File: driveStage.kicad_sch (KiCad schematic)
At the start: 57 parts, among them J1 MOD_IN, J2 DNP, J3 DNP, Q1 CSD17507Q5A, SW1 SW_DIP_x03, U1 LTC6655BHLS8-4.096, U2 MAX5719xSD, U3 ADA4898-1YRDZ, U4 ADA4898-1YRDZ, U5 RS8552, U6 ADA4898-1YRDZ

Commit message: complete placement
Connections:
- net GND: no longer J3.1 (In), R13.3
- new net: J3.1 (In), R13.3
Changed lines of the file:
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@@
   (junction (at 71.12 106.68) (diameter 0) (color 0 0 0 0)
   )
-  (junction (at 374.65 124.46) (diameter 0) (color 0 0 0 0)
-  )
   (junction (at 334.01 78.74) (diameter 0) (color 0 0 0 0)
   )
@@
   )
   (junction (at 118.11 119.38) (diameter 0) (color 0 0 0 0)
-  )
-  (junction (at 368.3 124.46) (diameter 0) (color 0 0 0 0)
   )
   (junction (at 341.63 196.85) (diameter 0) (color 0 0 0 0)
@@
     (stroke (width 0) (type default) (color 0 0 0 0))
   )
-  (wire (pts (xy 368.3 121.92) (xy 368.3 124.46))
+  (wire (pts (xy 368.3 121.92) (xy 368.3 161.29))
     (stroke (width 0) (type default) (color 0 0 0 0))
   )
@@
     (stroke (width 0) (type default) (color 0 0 0 0))
   )
-  (wire (pts (xy 368.3 124.46) (xy 368.3 161.29))
-    (stroke (width 0) (type default) (color 0 0 0 0))
-  )
   (wire (pts (xy 205.74 114.3) (xy 210.82 114.3))
     (stroke (width 0) (type default) (color 0 0 0 0))
@@
     (stroke (width 0) (type default) (color 0 0 0 0))
   )
-  (wire (pts (xy 368.3 124.46) (xy 374.65 124.46))
-    (stroke (width 0) (type default) (color 0 0 0 0))
-  )

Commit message: more routing
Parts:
- removed TP1, TP2, TP3, TP36, TP37, TP38, TP4, TP5, TP6, TP7, TP8: TestPoint, TestPoint:TestPoint_Pad_2.0x2.0mm, symbol Connector:TestPoint

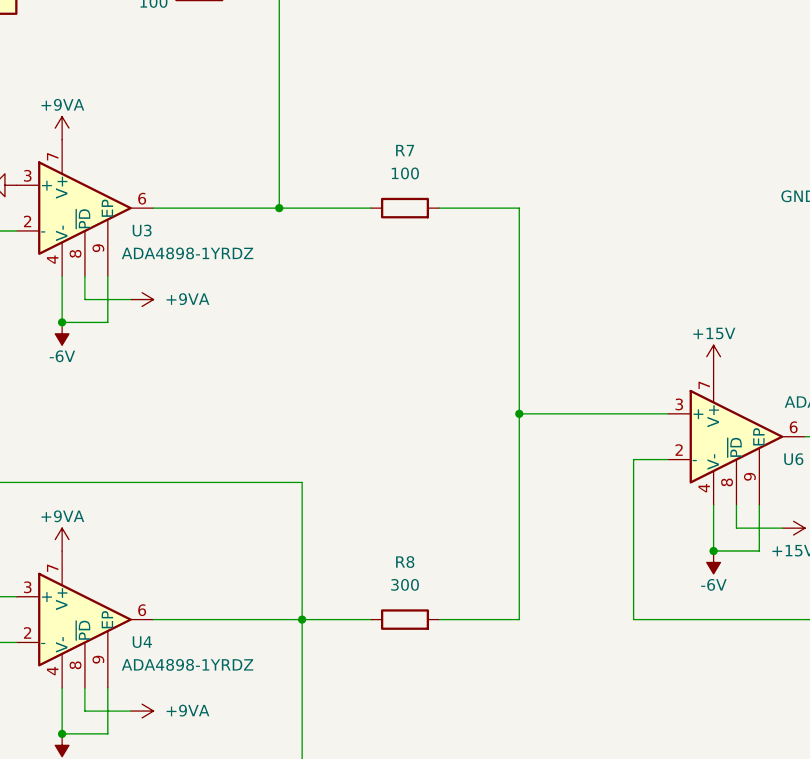
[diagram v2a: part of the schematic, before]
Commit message: add V01 production files, bug fixes
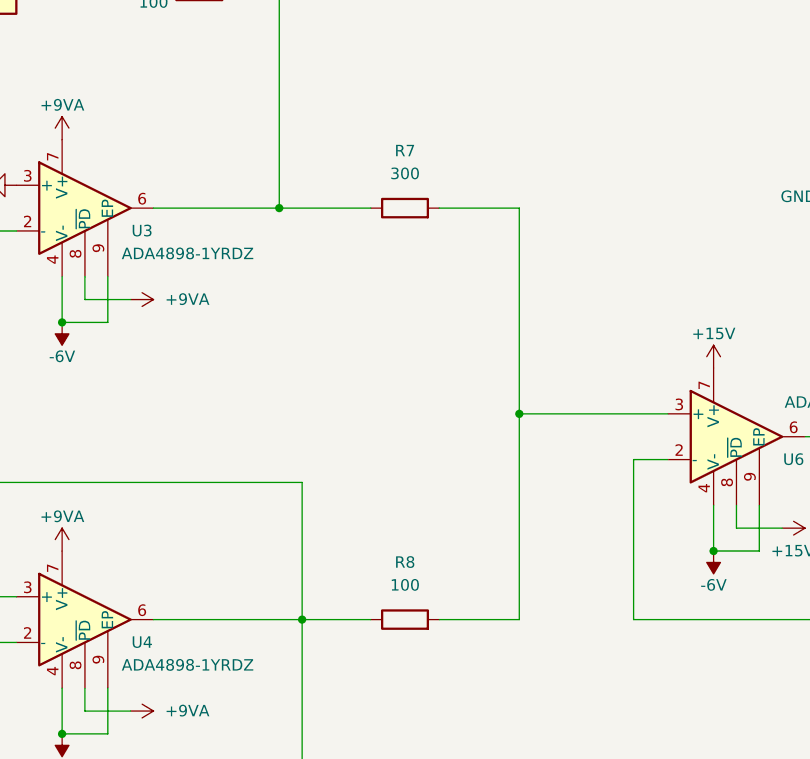
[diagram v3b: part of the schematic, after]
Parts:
- R7: value 100 -> 300
- R8: value 300 -> 100
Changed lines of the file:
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@@
     (in_bom yes) (on_board yes) (fields_autoplaced)
     (property "Reference" "R8" (id 0) (at 284.48 110.49 90))
-    (property "Value" "300" (id 1) (at 284.48 113.03 90))
+    (property "Value" "100" (id 1) (at 284.48 113.03 90))
     (property "Footprint" "Resistor_SMD:R_0603_1608Metric" (id 2) (at 284.48 118.618 90)
       (effects (font (size 1.27 1.27)) hide)
@@
     (in_bom yes) (on_board yes) (fields_autoplaced)
     (property "Reference" "R7" (id 0) (at 284.48 64.77 90))
-    (property "Value" "100" (id 1) (at 284.48 67.31 90))
+    (property "Value" "300" (id 1) (at 284.48 67.31 90))
     (property "Footprint" "Resistor_SMD:R_0603_1608Metric" (id 2) (at 284.48 72.898 90)
       (effects (font (size 1.27 1.27)) hide)

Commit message: v 0.2 schematics
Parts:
- removed J2, J3: DNP, Connector_Coaxial:U.FL_Hirose_U.FL-R-SMT-1_Vertical, symbol Connector:Conn_Coaxial
- removed R1: 50, Resistor_SMD:R_0805_2012Metric, symbol Device:R
- removed R2, R6: 100, Resistor_SMD:R_0603_1608Metric, symbol Device:R
- removed R5: 10, Resistor_SMD:R_0603_1608Metric, symbol Device:R
- added C? (x2): DNP, Capacitor_SMD:C_0603_1608Metric, symbol Device:C
- added C?: 10u PP, Capacitor_SMD:C_1812_4532Metric, symbol Device:C
- added C? (x2): 100n PPS, Capacitor_SMD:C_1210_3225Metric, symbol Device:C
- added R? (x2): DNP, Resistor_SMD:R_0603_1608Metric, symbol Device:R
- added R? (x2): 10, Resistor_SMD:R_0603_1608Metric, symbol Device:R
- added R?: 99, symbol Device:R
- added R?: 90, symbol Device:R
- added TP1, TP2, TP3, TP36, TP37, TP38, TP4: TestPoint, TestPoint:TestPoint_Pad_2.0x2.0mm, symbol Connector:TestPoint
- Q1: value CSD17507Q5A -> SQJA70EP-T1; MFR_PN CSD17507Q5A -> SQJA70EP-T1_GE3
- R13: footprint Resistor_SMD:R_Shunt_Ohmite_LVK20 -> kirdy:R_Shunt_VCS1625ZP
- R7: value 300 -> 100
- R8: value 100 -> 300
- renumbered C172 to C?
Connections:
- net DIN: now also TP3.1
- net GND: now also R13.3, R4.1, C?.2, C?.2, C?.2, R?.1; no longer U3.3 (+)
- net LD-: now also R?.2
- net PD_BIAS: now also TP38.1
- net PD_C: now also TP37.1
- net PD_MON: now also TP36.1
- net SCLK: now also TP2.1
- net ~{CS}: now also TP4.1
- net ~{LDAC}: now also TP1.1
- net at SW1.4: now also SW1.5, SW1.6, U3.3 (+)
- net at R7.1, U3.6: now also U3.2 (-); no longer R4.2
- net at R10.2, R11.1, TP9.1: now also C?.2
- net at C13.2, R10.1, U6.2 (-): now also R?.1, R?.1
- net at R7.2, R8.2, U6.3 (+): now also C?.1, C?.1
- net at C13.1, Q1.4 (G), U6.6: now also C?.1
- net at J1.1 (In): now also D1.2 (A2), SW1.1, R?.1, R?.1
- new net: C?.2, R?.2
- new net: C?.1, R?.1
- new net: R?.2, R?.2, SW1.2
- new net: R4.2, R?.2, SW1.3
- new net: C?.1, R?.2
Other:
- note removed: "For noise measurement"
- moved on the sheet: C1, C10, C11, C12, C13, C15, C16, C2, C3, C4, C5, C6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

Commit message: fixes
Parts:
- removed C?: 100n PPS, Capacitor_SMD:C_1210_3225Metric, symbol Device:C
- removed TP1, TP2, TP3, TP4: TestPoint, TestPoint:TestPoint_Pad_2.0x2.0mm, symbol Connector:TestPoint
- added C?: 10u PP, Capacitor_SMD:C_1812_4532Metric, symbol Device:C
- added R?: 100, Resistor_SMD:R_0603_1608Metric, symbol Device:R
- R7: value 100 -> 300
- R8: value 300 -> 100
- R?: value 10 -> 3.3; MFR_PN RT0603BRD0710RL -> (none); MFR_PN_ALT WR06X10R0FTL -> (none)
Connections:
- net GND: now also C?.2
- net at C5.2, R8.1, U4.2 (-): now also C?.1, C?.1, R?.2; no longer U4.6
- net at R?.1: now also C?.1
- net at R7.2, R8.2, U6.3 (+): no longer C?.1, C?.1
- new net: R?.1, U4.6
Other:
- moved on the sheet: C?, R8

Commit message: compensation
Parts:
- added C?: 1n6, Capacitor_SMD:C_0603_1608Metric, symbol Device:C
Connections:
- net at C5.2, C?.1, C?.1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: now also C?.1
- net at R?.1, U4.6: now also C?.2
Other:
- moved on the sheet: R?
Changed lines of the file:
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@@
   (junction (at 347.98 229.87) (diameter 0) (color 0 0 0 0)
   )
+  (junction (at 223.52 116.84) (diameter 0) (color 0 0 0 0)
+  )
   (junction (at 351.79 205.74) (diameter 0) (color 0 0 0 0)
   )
@@
   )
   (junction (at 116.84 127) (diameter 0) (color 0 0 0 0)
+  )
+  (junction (at 229.87 137.16) (diameter 0) (color 0 0 0 0)
   )
   (junction (at 24.13 106.68) (diameter 0) (color 0 0 0 0)
@@
     (stroke (width 0) (type default) (color 0 0 0 0))
   )
-  (wire (pts (xy 213.36 127) (xy 218.44 127))
+  (wire (pts (xy 213.36 127) (xy 217.17 127))
     (stroke (width 0) (type default) (color 0 0 0 0))
   )
@@
     (stroke (width 0) (type default) (color 0 0 0 0))
   )
+  (wire (pts (xy 229.87 137.16) (xy 237.49 137.16))
+    (stroke (width 0) (type default) (color 0 0 0 0))
+  )
   (wire (pts (xy 175.26 114.3) (xy 205.74 114.3))
     (stroke (width 0) (type default) (color 0 0 0 0))
@@
     (stroke (width 0) (type default) (color 0 0 0 0))
   )
-  (wire (pts (xy 233.68 116.84) (xy 237.49 116.84))
+  (wire (pts (xy 234.95 116.84) (xy 237.49 116.84))
     (stroke (width 0) (type default) (color 0 0 0 0))
   )
@@
     (stroke (width 0) (type default) (color 0 0 0 0))
   )
-  (wire (pts (xy 200.66 137.16) (xy 237.49 137.16))
+  (wire (pts (xy 200.66 137.16) (xy 229.87 137.16))
     (stroke (width 0) (type default) (color 0 0 0 0))
   )
@@
     (stroke (width 0) (type default) (color 0 0 0 0))
   )
+  (wire (pts (xy 229.87 120.65) (xy 223.52 120.65))
+    (stroke (width 0) (type default) (color 0 0 0 0))
+  )
   (wire (pts (xy 88.9 106.68) (xy 104.14 106.68))
     (stroke (width 0) (type default) (color 0 0 0 0))
@@
     (stroke (width 0) (type default) (color 0 0 0 0))
   )
+  (wire (pts (xy 223.52 120.65) (xy 223.52 116.84))
+    (stroke (width 0) (type default) (color 0 0 0 0))
+  )
   (wire (pts (xy 341.63 109.22) (xy 341.63 116.84))
     (stroke (width 0) (type default) (color 0 0 0 0))
@@
     (stroke (width 0) (type default) (color 0 0 0 0))
   )
+  (wire (pts (xy 229.87 130.81) (xy 229.87 137.16))
+    (stroke (width 0) (type default) (color 0 0 0 0))
+  )
   (wire (pts (xy 299.72 63.5) (xy 299.72 64.77))
     (stroke (width 0) (type default) (color 0 0 0 0))
@@
     (stroke (width 0) (type default) (color 0 0 0 0))
   )
+  (wire (pts (xy 223.52 116.84) (xy 227.33 116.84))
+    (stroke (width 0) (type default) (color 0 0 0 0))
+  )
   (wire (pts (xy 360.68 124.46) (xy 367.03 124.46))
     (stroke (width 0) (type default) (color 0 0 0 0))
@@
     (stroke (width 0) (type default) (color 0 0 0 0))
   )
+  (wire (pts (xy 229.87 123.19) (xy 229.87 120.65))
+    (stroke (width 0) (type default) (color 0 0 0 0))
+  )
   (wire (pts (xy 285.75 73.66) (xy 299.72 73.66))
     (stroke (width 0) (type default) (color 0 0 0 0))
   )
-  (wire (pts (xy 220.98 116.84) (xy 226.06 116.84))
+  (wire (pts (xy 220.98 116.84) (xy 223.52 116.84))
     (stroke (width 0) (type default) (color 0 0 0 0))
   )
@@
   (symbol (lib_id "Amplifier_Operational:ADA4898-1YRDZ") (at 213.36 116.84 0) (unit 1)
     (in_bom yes) (on_board yes)
-    (property "Reference" "U4" (id 0) (at 219.71 119.38 0))
-    (property "Value" "ADA4898-1YRDZ" (id 1) (at 224.79 121.92 0))
+    (property "Reference" "U4" (id 0) (at 218.44 110.49 0))
+    (property "Value" "ADA4898-1YRDZ" (id 1) (at 223.52 107.95 0))
     (property "Footprint" "Package_SO:SOIC-8-1EP_3.9x4.9mm_P1.27mm_EP2.29x3mm" (id 2) (at 213.36 132.08 0)
       (effects (font (size 1.27 1.27)) hide)
@@
     (pin "2")
   )
+  (symbol (lib_id "Device:C") (at 229.87 127 180) (unit 1)
+    (in_bom yes) (on_board yes)
+    (property "Reference" "C?" (id 0) (at 234.95 125.73 0))
+    (property "Value" "1n6" (id 1) (at 234.95 128.27 0))
+    (property "Footprint" "Capacitor_SMD:C_0603_1608Metric" (id 2) (at 228.9048 123.19 0)
+      (effects (font (size 1.27 1.27)) hide)
+    )
+    (property "Datasheet" "~" (id 3) (at 229.87 127 0)
+      (effects (font (size 1.27 1.27)) hide)
+    )
+    (property "MFR_PN" "GCM1885C1H162FA16D" (id 4) (at 229.87 127 0)
+      (effects (font (size 1.27 1.27)) hide)
+    )
+    (property "MFR_PN_ALT" "C0603C162J5GAC7867" (id 5) (at 229.87 127 0)
+      (effects (font (size 1.27 1.27)) hide)
+    )
+    (pin "1")
+    (pin "2")
+  )
   (symbol (lib_id "Device:C") (at 222.25 148.59 90) (unit 1)
     (in_bom yes) (on_board yes)
@@
     (pin "2")
   )
-  (symbol (lib_id "power:+9VA") (at 218.44 127 270) (unit 1)
-    (in_bom yes) (on_board yes) (fields_autoplaced)
-    (property "Reference" "#PWR021" (id 0) (at 215.265 127 0)
-      (effects (font (size 1.27 1.27)) hide)
-    )
-    (property "Value" "+9VA" (id 1) (at 222.25 126.9999 90)
-      (effects (font (size 1.27 1.27)) (justify left))
-    )
-    (property "Footprint" "" (id 2) (at 218.44 127 0)
-      (effects (font (size 1.27 1.27)) hide)
-    )
-    (property "Datasheet" "" (id 3) (at 218.44 127 0)
+  (symbol (lib_id "power:+9VA") (at 217.17 127 270) (unit 1)
+    (in_bom yes) (on_board yes) (fields_autoplaced)
+    (property "Reference" "#PWR021" (id 0) (at 213.995 127 0)
+      (effects (font (size 1.27 1.27)) hide)
+    )
+    (property "Value" "+9VA" (id 1) (at 220.98 126.9999 90)
+      (effects (font (size 1.27 1.27)) (justify left))
+    )
+    (property "Footprint" "" (id 2) (at 217.17 127 0)
+      (effects (font (size 1.27 1.27)) hide)
+    )
+    (property "Datasheet" "" (id 3) (at 217.17 127 0)
       (effects (font (size 1.27 1.27)) hide)
     )
@@
     (pin "2")
   )
-  (symbol (lib_id "Device:R") (at 229.87 116.84 90) (unit 1)
-    (in_bom yes) (on_board yes) (fields_autoplaced)
-    (property "Reference" "R?" (id 0) (at 229.87 110.49 90))
-    (property "Value" "100" (id 1) (at 229.87 113.03 90))
-    (property "Footprint" "Resistor_SMD:R_0603_1608Metric" (id 2) (at 229.87 118.618 90)
-      (effects (font (size 1.27 1.27)) hide)
-    )
-    (property "Datasheet" "~" (id 3) (at 229.87 116.84 0)
-      (effects (font (size 1.27 1.27)) hide)
-    )
-    (property "MFR_PN" "RT0603FRE07300RL" (id 4) (at 229.87 116.84 0)
-      (effects (font (size 1.27 1.27)) hide)
-    )
-    (property "MFR_PN_ALT" "RC0603FR-10300RL" (id 5) (at 229.87 116.84 0)
-      (effects (font (size 1.27 1.27)) hide)
-    )
+  (symbol (lib_id "Device:R") (at 231.14 116.84 90) (unit 1)
+    (in_bom yes) (on_board yes)
+    (property "Reference" "R?" (id 0) (at 231.14 111.76 90))
+    (property "Value" "100" (id 1) (at 231.14 114.3 90))
+    (property "Footprint" "Resistor_SMD:R_0603_1608Metric" (id 2) (at 231.14 118.618 90)
+      (effects (font (size 1.27 1.27)) hide)
+    )
+    (property "Datasheet" "~" (id 3) (at 231.14 116.84 0)
+      (effects (font (size 1.27 1.27)) hide)
+    )
+    (property "MFR_PN" "RT0603FRE07300RL" (id 4) (at 231.14 116.84 0)
+      (effects (font (size 1.27 1.27)) hide)
+    )
+    (property "MFR_PN_ALT" "RC0603FR-10300RL" (id 5) (at 231.14 116.84 0)
+      (effects (font (size 1.27 1.27)) hide)
+    )

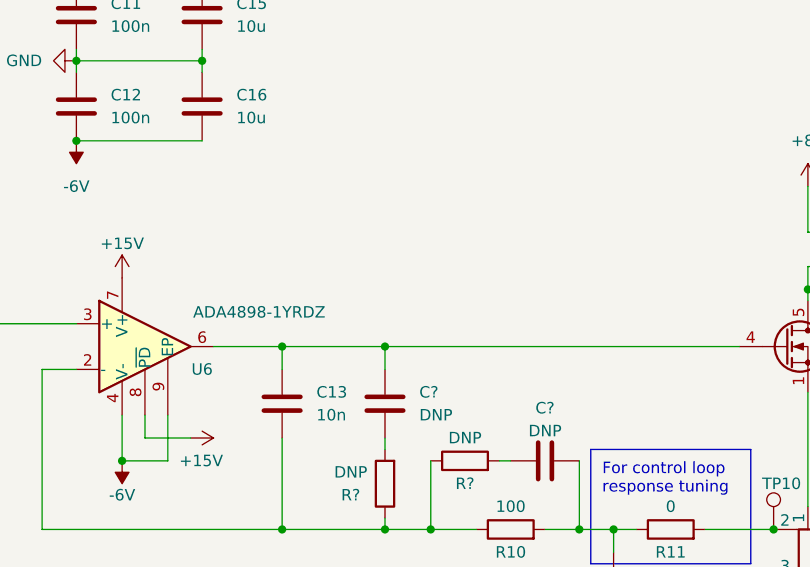
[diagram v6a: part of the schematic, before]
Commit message: add gate pull down
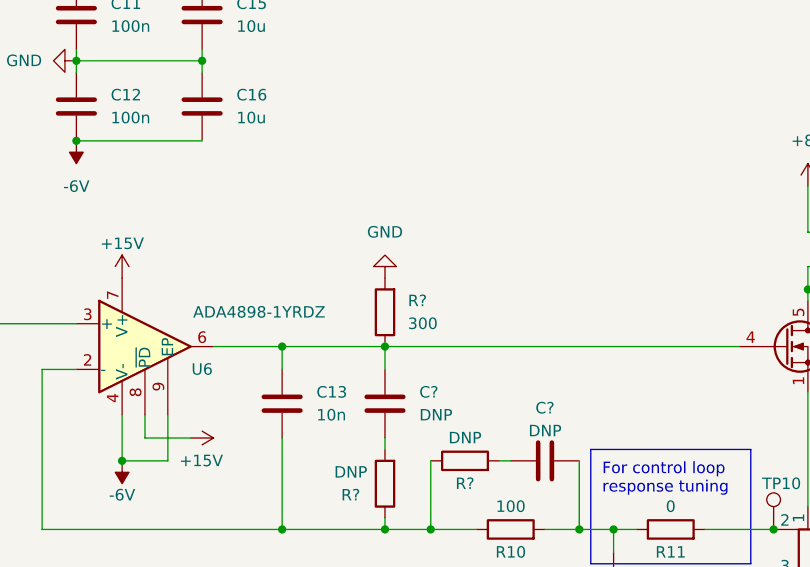
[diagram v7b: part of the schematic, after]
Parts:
- added R?: 300, Resistor_SMD:R_0603_1608Metric, symbol Device:R
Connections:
- net GND: now also R?.2
- net at C13.1, C?.1, Q1.4 (G)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: now also R?.1
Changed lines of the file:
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@@
+    (pin "2")
+  )
+  (symbol (lib_id "Device:R") (at 320.04 92.71 180) (unit 1)
+    (in_bom yes) (on_board yes) (fields_autoplaced)
+    (property "Reference" "R?" (id 0) (at 322.58 91.4399 0)
+      (effects (font (size 1.27 1.27)) (justify right))
+    )
+    (property "Value" "300" (id 1) (at 322.58 93.9799 0)
+      (effects (font (size 1.27 1.27)) (justify right))
+    )
+    (property "Footprint" "Resistor_SMD:R_0603_1608Metric" (id 2) (at 321.818 92.71 90)
+      (effects (font (size 1.27 1.27)) hide)
+    )
+    (property "Datasheet" "~" (id 3) (at 320.04 92.71 0)
+      (effects (font (size 1.27 1.27)) hide)
+    )
+    (property "MFR_PN" "WR06X1000FTL" (id 4) (at 320.04 92.71 0)
+      (effects (font (size 1.27 1.27)) hide)
+    )
+    (property "MFR_PN_ALT" "RMCF0603FT100R" (id 5) (at 320.04 92.71 0)
+      (effects (font (size 1.27 1.27)) hide)
+    )
+    (pin "1")
     (pin "2")
   )
@@
     (pin "2")
   )
+  (symbol (lib_id "power:GND") (at 320.04 88.9 180) (unit 1)
+    (in_bom yes) (on_board yes) (fields_autoplaced)
+    (property "Reference" "#PWR?" (id 0) (at 320.04 82.55 0)
+      (effects (font (size 1.27 1.27)) hide)
+    )
+    (property "Value" "GND" (id 1) (at 320.04 83.82 0))
+    (property "Footprint" "" (id 2) (at 320.04 88.9 0)
+      (effects (font (size 1.27 1.27)) hide)
+    )
+    (property "Datasheet" "" (id 3) (at 320.04 88.9 0)
+      (effects (font (size 1.27 1.27)) hide)
+    )
+    (pin "1")
+  )
   (symbol (lib_id "Device:C") (at 245.11 123.19 0) (unit 1)
